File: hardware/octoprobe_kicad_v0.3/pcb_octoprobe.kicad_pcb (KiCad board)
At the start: 2 copper layers, 100 x 160 mm, 659 parts, among them J1001 Conn_01x20, J1002 Conn_01x20, J102 USB-226-BRW, J1101 Conn_01x20, J1102 Conn_01x20, J1103 Conn_01x20, J201 BOOT Button, J801 USB_C_Receptacle_USB2.0, Q201 NMOS, Q202 NMOS, SW201 RESET, U1001 GAQY221S, U1201 MT9700, U1401 GAQY221S, U201 RP2040, U202 AMS1117-3.3, U203 W25Q128JVS, U301 GAQY221S, U401 GAQY221S, U501 GAQY221S, U601 GAQY221S, U701 GAQY221S, U801 AMS1117-3.3, U802 USB2514B_Bi, U901 MT9700, X201 Oscillator-12MHz, Y801 24MHz

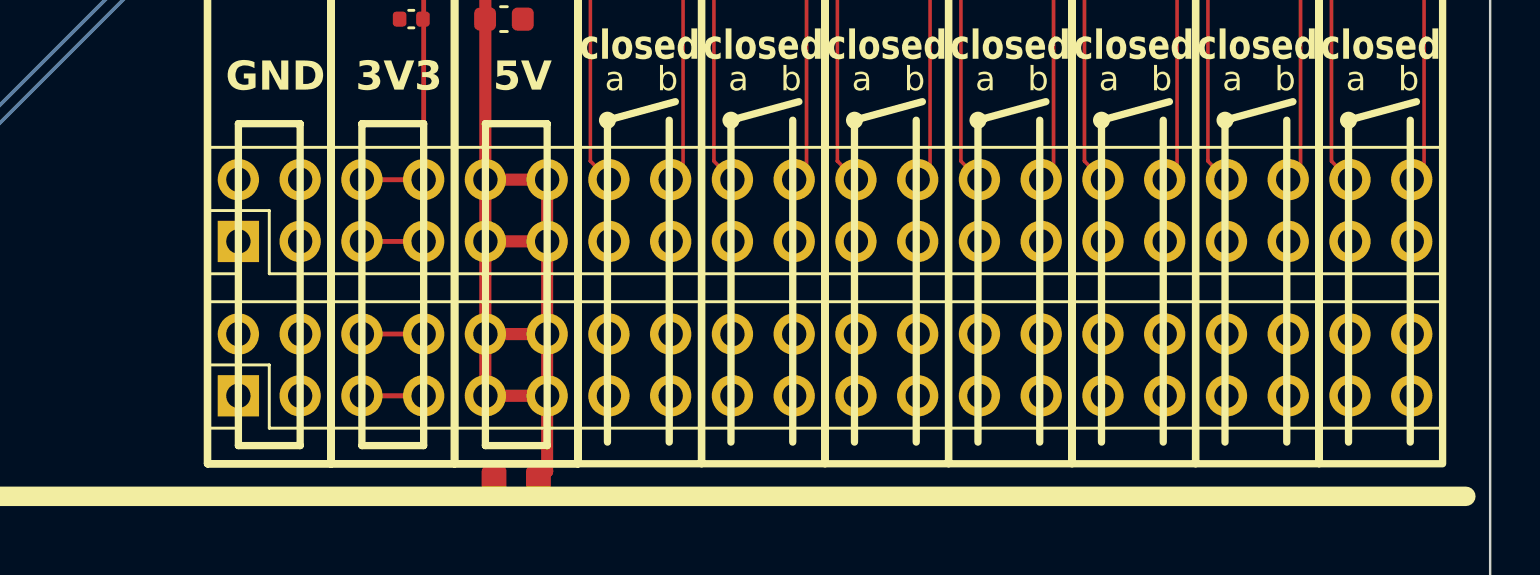
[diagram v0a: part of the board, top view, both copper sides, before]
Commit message: PCB: Add "Open Hardware"
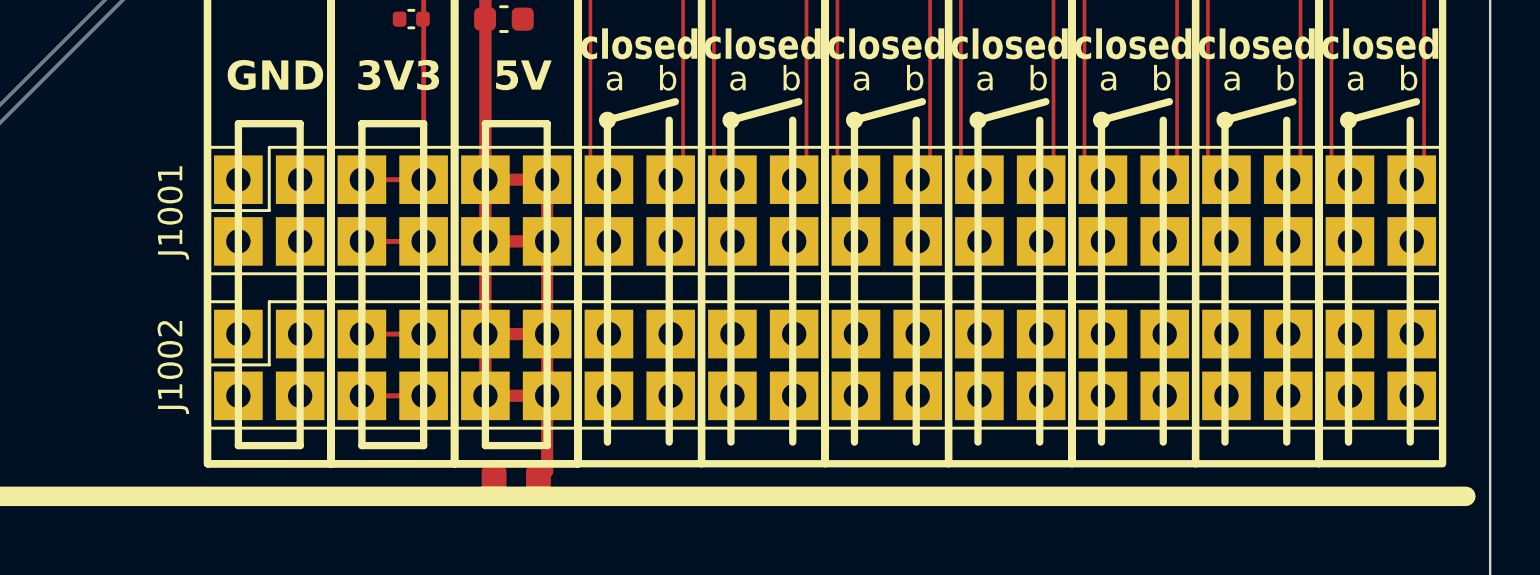
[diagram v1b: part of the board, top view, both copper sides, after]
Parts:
- J1001, J1002: footprint 00_project_library:PinSocket_2x20_P2.54mm_Vertical-mirrored -> 00_project_library:PinSocket_2x20_P2.54mm_Vertical_squarepad

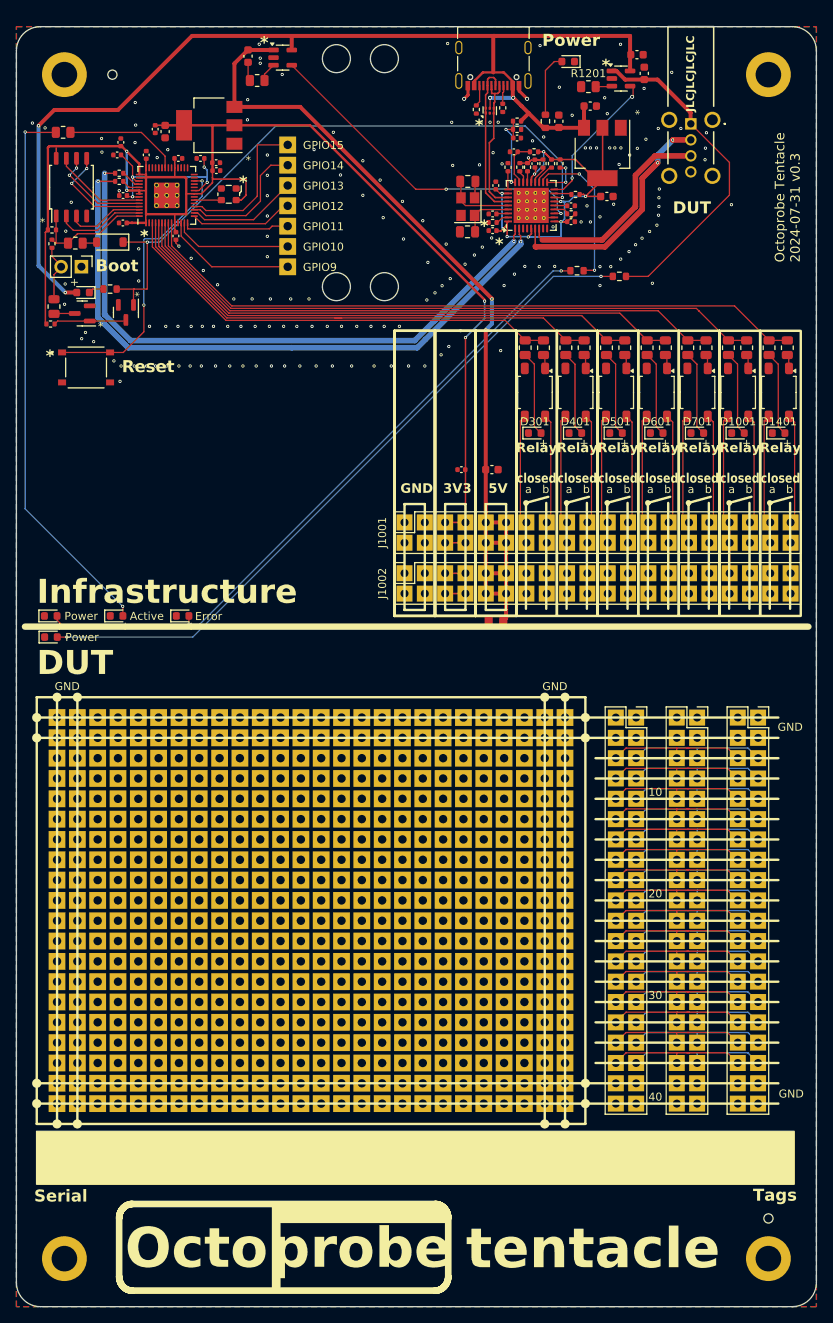
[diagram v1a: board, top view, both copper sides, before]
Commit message: PCB: Production files ready
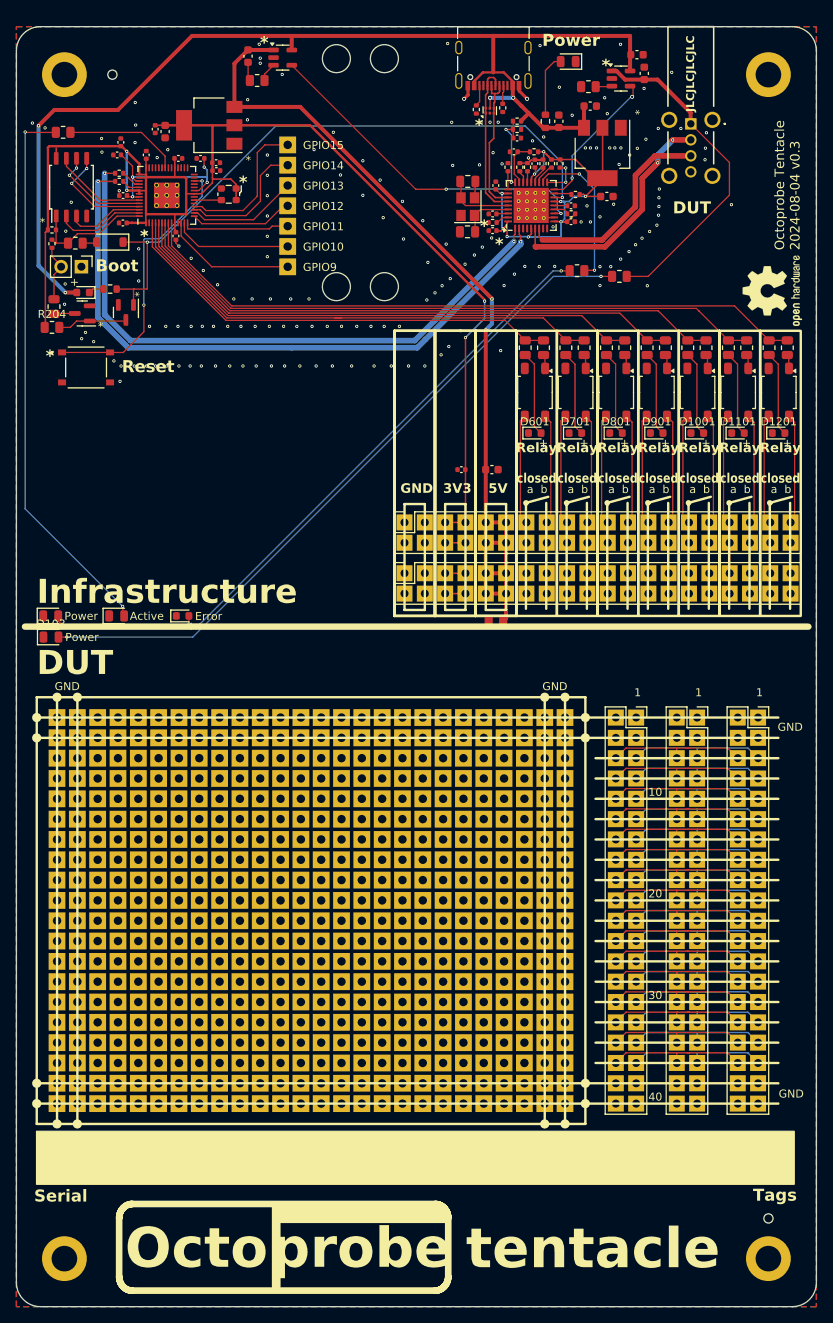
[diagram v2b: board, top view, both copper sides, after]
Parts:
- added Logo_open_hardware101: Logo_Open_Hardware_Small, Symbol:OSHW-Logo2_9.8x8mm_SilkScreen, F.Cu at (168.5, 65.5)
- D103, D104, D201: footprint 00_project_library:LED_0603_1608Metric -> LED_SMD:LED_0805_2012Metric
- D301: renamed from D801; footprint 00_project_library:LED_0603_1608Metric -> LED_SMD:LED_0805_2012Metric
- R102, R103: footprint Resistor_SMD:R_0603_1608Metric -> Resistor_SMD:R_0805_2012Metric
- R204: renamed from R205; footprint Resistor_SMD:R_0402_1005Metric -> Resistor_SMD:R_0805_2012Metric
- moved R204 0.46 mm to (78.4, 70.1)
- renumbered BP1101 to BP1301, BP1102 to BP1302, C1201 to C1401, C1202 to C1402, C203 to C201, C204 to C202, C205 to C203, C206 to C204, C207 to C205, C208 to C206, C209 to C207, C210 to C208, C211 to C209, C212 to C210, C213 to C211, C214 to C212, C215 to C213, C216 to C214, C801 to C301, C802 to C302, C803 to C303, C804 to C304, C805 to C305, C806 to C306, C807 to C307, C808 to C308, C809 to C309, C810 to C310, C811 to C311, C812 to C312, C901 to C401, C902 to C402, D701 to D1001, D1001 to D1101, D1401 to D1201, D802 to D302, D301 to D601, D401 to D701, D501 to D801, D601 to D901, H1101 to H1301, H1102 to H1302, H1103 to H1303, H1104 to H1304, H1105 to H1305, H1106 to H1306, H1107 to H1307, H1108 to H1308, J102 to J101, J1101 to J1301, J1102 to J1302, J1103 to J1303, J801 to J301, J1001 to J501, J1002 to J502, R701 to R1001, R702 to R1002, R1001 to R1101, R1002 to R1102, R1401 to R1201, R1402 to R1202, R1201 to R1401, R202 to R201, R203 to R202, R204 to R203, R206 to R205, R207 to R206, R208 to R207, R209 to R208, R801 to R301, R802 to R302, R803 to R303, R804 to R304, R805 to R305, R806 to R306, R807 to R307, R808 to R308, R809 to R309, R810 to R310, R811 to R311, R812 to R312, R813 to R313, R814 to R314, R815 to R315, R901 to R401, R301 to R601, R302 to R602, R401 to R701, R402 to R702, R501 to R801, R502 to R802, R601 to R901, R602 to R902, TH1101 to TH1301, TH1102 to TH1302, U701 to U1001, U1001 to U1101, U1401 to U1201, U1201 to U1401, U801 to U301, U802 to U302, U901 to U401, U301 to U601, U401 to U701, U501 to U801, U601 to U901, UR701 to UR1001, UR1001 to UR1101, UR1401 to UR1201, UR301 to UR601, UR401 to UR701, UR501 to UR801, UR601 to UR901, Y801 to Y301
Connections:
- X201 pad 1: unconnected-(X201-OE-Pad1) -> +3V3
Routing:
- net +3V3: track 201.7 -> 199.7 mm
- net Net-(U201-GPIO15): track 19.1 -> 18.5 mm
